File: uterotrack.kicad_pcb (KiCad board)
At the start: 4 copper layers, 34 x 98 mm, 139 parts, among them J1 RFShield, J2 MicroSD_Card, J3 Argos_Prog, J4 AS5510, J5 Prog, J6 EXP, Q1 DMP2110UW, Q10 MMBT2222, Q11 MMBT2222, Q12 MMBT2222, Q13 MMBT2222, Q14 SiS454DN, Q15 SiS454DN, Q16 SiS415DNT, Q17 MMBT4403, Q18 MMBT2222, Q2 DMP2110UW, Q3 MMBT2222, Q4 DMP2110UW, Q5 DMP2110UW, Q6 MMBT2222, Q7 SiS415DNT, Q8 DMP2110UW, Q9 MMBT2222, U1 Argos_SMD, U10 AH1806-W, U11 LTC3221EDC-3.3, U2 ESP32-S3-WROOM-1, U3 keller_6LHPD, U4 RV-3032-C7, U5 CAM-M8Q, U6 BQ29732, U7 BQ51050BRHL, U8 TPS63001, U9 TPS63900

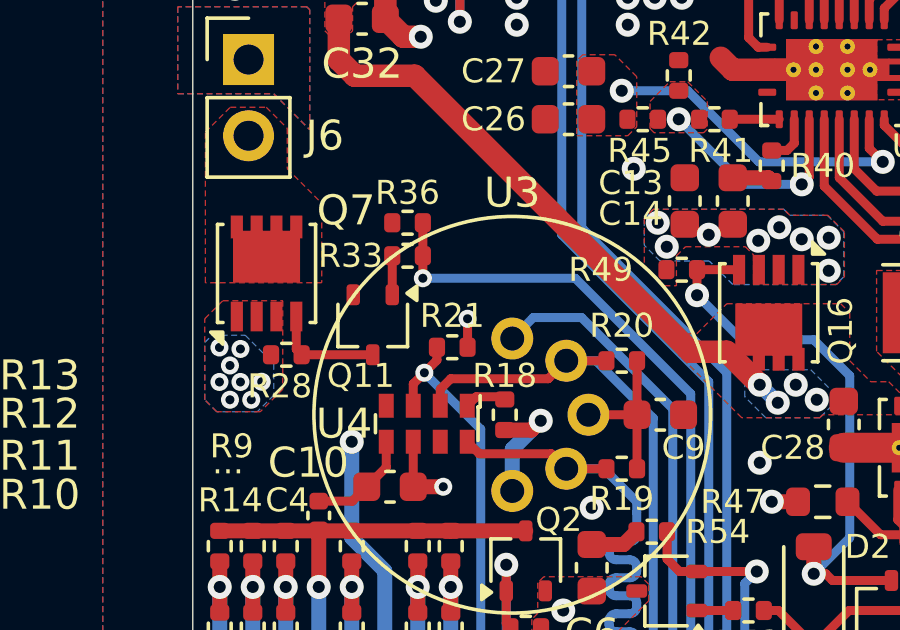
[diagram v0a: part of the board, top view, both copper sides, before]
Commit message: Fix VIAs for BATT, EXP_EN, RTC_INT and 3V3 near of previous.
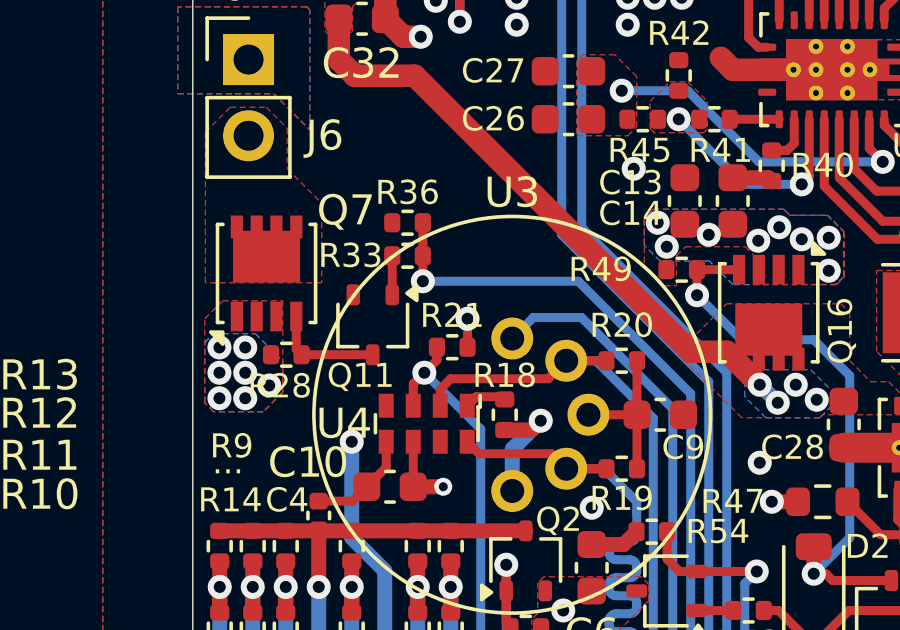
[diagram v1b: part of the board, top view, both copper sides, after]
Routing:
- net /Batt: track 176.3 -> 176.4 mm, vias 36 -> 35
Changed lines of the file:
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@@
 	)
 	(via
-		(at 133.89 113.6075)
-		(size 0.6)
-		(drill 0.3)
+		(at 135.55 113.725)
+		(size 0.8)
+		(drill 0.4)
 		(layers "F.Cu" "B.Cu")
 		(net 3)
 	)
 	(via
-		(at 150.45 82.3)
+		(at 133.89 113.3)
 		(size 0.8)
 		(drill 0.4)
@@
 	)
 	(via
-		(at 161.1 80.1)
+		(at 150.45 82.3)
 		(size 0.8)
 		(drill 0.4)
@@
 	)
 	(via
-		(at 134.24 114.2)
-		(size 0.6)
-		(drill 0.3)
+		(at 161.1 80.1)
+		(size 0.8)
+		(drill 0.4)
 		(layers "F.Cu" "B.Cu")
 		(net 3)
@@
 	)
 	(via
-		(at 134.24 113.0575)
-		(size 0.6)
-		(drill 0.3)
+		(at 161.1 74.5)
+		(size 0.8)
+		(drill 0.4)
 		(layers "F.Cu" "B.Cu")
 		(net 3)
 	)
 	(via
-		(at 161.1 74.5)
+		(at 149.1 81.4)
 		(size 0.8)
 		(drill 0.4)
@@
 	)
 	(via
-		(at 149.1 81.4)
+		(at 134.75 112.4575)
 		(size 0.8)
 		(drill 0.4)
@@
 	)
 	(via
-		(at 134.59 113.6075)
-		(size 0.6)
-		(drill 0.3)
-		(layers "F.Cu" "B.Cu")
-		(net 3)
-	)
-	(via
 		(at 148.2 81.4)
 		(size 0.8)
@@
 	)
 	(via
+		(at 134.75 113.3)
+		(size 0.8)
+		(drill 0.4)
+		(layers "F.Cu" "B.Cu")
+		(net 3)
+	)
+	(via
+		(at 134.75 114.15)
+		(size 0.8)
+		(drill 0.4)
+		(layers "F.Cu" "B.Cu")
+		(net 3)
+	)
+	(via
 		(at 150 81.4)
 		(size 0.8)
@@
 	)
 	(via
-		(at 134.59 112.5075)
-		(size 0.6)
-		(drill 0.3)
+		(at 133.89 114.15)
+		(size 0.8)
+		(drill 0.4)
 		(layers "F.Cu" "B.Cu")
 		(net 3)
@@
 	(via
 		(at 133.89 112.4575)
-		(size 0.6)
-		(drill 0.3)
-		(layers "F.Cu" "B.Cu")
-		(net 3)
-	)
-	(via
-		(at 134.95 114.2)
-		(size 0.6)
-		(drill 0.3)
+		(size 0.8)
+		(drill 0.4)
 		(layers "F.Cu" "B.Cu")
 		(net 3)
@@
 	)
 	(via
-		(at 135.3 113.6)
-		(size 0.6)
-		(drill 0.3)
-		(layers "F.Cu" "B.Cu")
-		(net 3)
-	)
-	(via
 		(at 141.35 117.1)
 		(size 0.6)
@@
 	)
 	(segment
-		(start 139.4 121.85)
-		(end 135.1 126.15)
+		(start 148.79 108.45)
+		(end 138.7575 108.45)
+		(width 1.5)
+		(layer "In2.Cu")
+		(net 3)
+	)
+	(segment
+		(start 141.35 116.15)
+		(end 141.35 117.1)
 		(width 0.75)
 		(layer "In2.Cu")
@@
 	)
 	(segment
-		(start 135.1 130.3)
-		(end 139.875 135.075)
+		(start 139.4 121.85)
+		(end 135.1 126.15)
 		(width 0.75)
 		(layer "In2.Cu")
@@
 	)
 	(segment
-		(start 148.79 108.45)
-		(end 138.8475 108.45)
-		(width 1.5)
+		(start 135.1 130.3)
+		(end 139.875 135.075)
+		(width 0.75)
 		(layer "In2.Cu")
 		(net 3)
@@
 	)
 	(segment
-		(start 138.8475 108.45)
-		(end 134.24 113.0575)
-		(width 1.5)
+		(start 166 146.8)
+		(end 166 132)
+		(width 0.5)
 		(layer "In2.Cu")
 		(net 3)
 	)
 	(segment
-		(start 166 146.8)
-		(end 166 132)
-		(width 0.5)
+		(start 134.75 112.4575)
+		(end 134.75 113.3)
+		(width 1.5)
 		(layer "In2.Cu")
 		(net 3)
@@
 	)
 	(segment
-		(start 141.35 116.15)
-		(end 141.35 117.1)
-		(width 0.75)
-		(layer "In2.Cu")
-		(net 3)
-	)
-	(segment
 		(start 139.875 135.075)
 		(end 139.875 138.22)
@@
 	)
 	(segment
-		(start 138.8075 113.6075)
-		(end 141.35 116.15)
+		(start 135.1 126.15)
+		(end 135.1 130.3)
 		(width 0.75)
 		(layer "In2.Cu")
@@
 	)
 	(segment
-		(start 135.1 126.15)
-		(end 135.1 130.3)
-		(width 0.75)
+		(start 138.7575 108.45)
+		(end 134.75 112.4575)
+		(width 1.5)
 		(layer "In2.Cu")
 		(net 3)
@@
 	)
 	(segment
+		(start 138.5 113.3)
+		(end 141.35 116.15)
+		(width 0.75)
+		(layer "In2.Cu")
+		(net 3)
+	)
+	(segment
+		(start 134.75 113.3)
+		(end 138.5 113.3)
+		(width 0.75)
+		(layer "In2.Cu")
+		(net 3)
+	)
+	(segment
 		(start 153.3 82)
 		(end 152.7 81.4)
@@
 	)
 	(segment
-		(start 134.59 113.6075)
-		(end 138.8075 113.6075)
-		(width 0.75)
-		(layer "In2.Cu")
-		(net 3)
-	)
-	(segment
 		(start 155 143.7)
 		(end 147.85 143.7)
@@
 	)
 	(segment
-		(start 142.16 112.45)
-		(end 142.16 111.5)
-		(width 0.3)
-		(layer "F.Cu")
-		(net 4)
-	)
-	(segment
 		(start 158.5 117.4)
 		(end 158.7 117.6)
@@
 		(net 4)
 	)
+	(segment
+		(start 142.16 112.45)
+		(end 142.16 111.5)
+		(width 0.3)
+		(layer "F.Cu")
+		(net 4)
+	)
 	(via
 		(at 145.35 121.225)
@@
 	(via
 		(at 142.16 111.5)
-		(size 0.6)
-		(drill 0.3)
+		(size 0.8)
+		(drill 0.4)
 		(layers "F.Cu" "B.Cu")
 		(net 4)
@@
 	(via
 		(at 140.72 113.3)
-		(size 0.6)
-		(drill 0.3)
+		(size 0.8)
+		(drill 0.4)
 		(layers "F.Cu" "B.Cu")
 		(net 88)
@@
 	)
 	(segment
+		(start 140.67 108.3)
+		(end 140.67 110.25)
+		(width 0.3)
+		(layer "F.Cu")
+		(net 93)
+	)
+	(segment
 		(start 143.54 136.5)
 		(end 142.85 135.81)
@@
 	)
 	(segment
-		(start 140.67 108.3)
-		(end 140.67 110.15)
-		(width 0.3)
-		(layer "F.Cu")
-		(net 93)
-	)
-	(segment
 		(start 142.85 135.81)
 		(end 141.65 135.81)
@@
 	)
 	(via
-		(at 140.67 110.15)
-		(size 0.6)
-		(drill 0.3)
+		(at 140.67 110.25)
+		(size 0.8)
+		(drill 0.4)
 		(layers "F.Cu" "B.Cu")
 		(net 93)
 	)
 	(segment
-		(start 149.6 133.5)
-		(end 149.6 114)
+		(start 145.85 110.25)
+		(end 140.67 110.25)
 		(width 0.3)
 		(layer "B.Cu")
@@
 	)
 	(segment
-		(start 145.75 110.15)
-		(end 140.67 110.15)
+		(start 149.6 114)
+		(end 145.85 110.25)
 		(width 0.3)
 		(layer "B.Cu")
@@
 	)
 	(segment
-		(start 149.6 114)
-		(end 145.75 110.15)
+		(start 149.6 133.5)
+		(end 149.6 114)
 		(width 0.3)
 		(layer "B.Cu")
@@
 		(polygon
 			(pts
-				(xy 136 110.9) (xy 136 113.85) (xy 135.25 114.6) (xy 133.8 114.6) (xy 133.4 114.2) (xy 133.4 111.5)
+				(xy 136 110.9) (xy 136 113.95) (xy 135.35 114.6) (xy 133.7 114.6) (xy 133.4 114.3) (xy 133.4 111.5)
 				(xy 134 110.9)
 			)
@@
 		(polygon
 			(pts
-				(xy 134.75 112.05) (xy 135.7 113) (xy 135.7 114.05) (xy 135.15 114.6) (xy 133.8 114.6) (xy 133.4 114.2)
-				(xy 133.4 112.29) (xy 133.64 112.05)
+				(xy 135.09 112) (xy 136 112.91) (xy 136 113.95) (xy 135.35 114.6) (xy 133.7 114.6) (xy 133.4 114.3)
+				(xy 133.4 112.29) (xy 133.69 112)
 			)
 		)
@@
 	)
 	(zone
+		(net 3)
+		(net_name "/Batt")
+		(layer "In1.Cu")
+		(hatch edge 0.5)
+		(priority 5)
+		(connect_pads yes
+			(clearance 0)
+		)
+		(min_thickness 0.254)
+		(filled_areas_thickness no)
+		(fill yes
+			(thermal_gap 0.5)
+			(thermal_bridge_width 0.5)
+		)
+		(polygon
+			(pts
+				(xy 135.09 112) (xy 136 112.91) (xy 136 113.95) (xy 135.35 114.6) (xy 133.7 114.6) (xy 133.4 114.3)
+				(xy 133.4 112.29) (xy 133.69 112)
+			)
+		)
+	)
+	(zone
 		(net 22)
 		(net_name "/BOut")
@@
 			)
 		)
+	)
+	(zone
+		(net 3)
+		(net_name "/Batt")
+		(layer "In2.Cu")
+		(hatch edge 0.5)
+		(priority 5)
+		(connect_pads yes
+			(clearance 0)
+		)
+		(min_thickness 0.254)
+		(filled_areas_thickness no)
+		(fill yes
+			(thermal_gap 0.5)
+			(thermal_bridge_width 0.5)
+		)
+		(polygon
+			(pts
+				(xy 135.807282 111.4) (xy 136.3 111.892718) (xy 136.3 113.65) (xy 135.35 114.6) (xy 133.7 114.6)
+				(xy 133.4 114.3) (xy 133.4 112.29) (xy 134.29 111.4)
+			)
+		)
